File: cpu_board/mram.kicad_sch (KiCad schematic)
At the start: 12 parts, among them U4 EM064LXQADG13IS1T

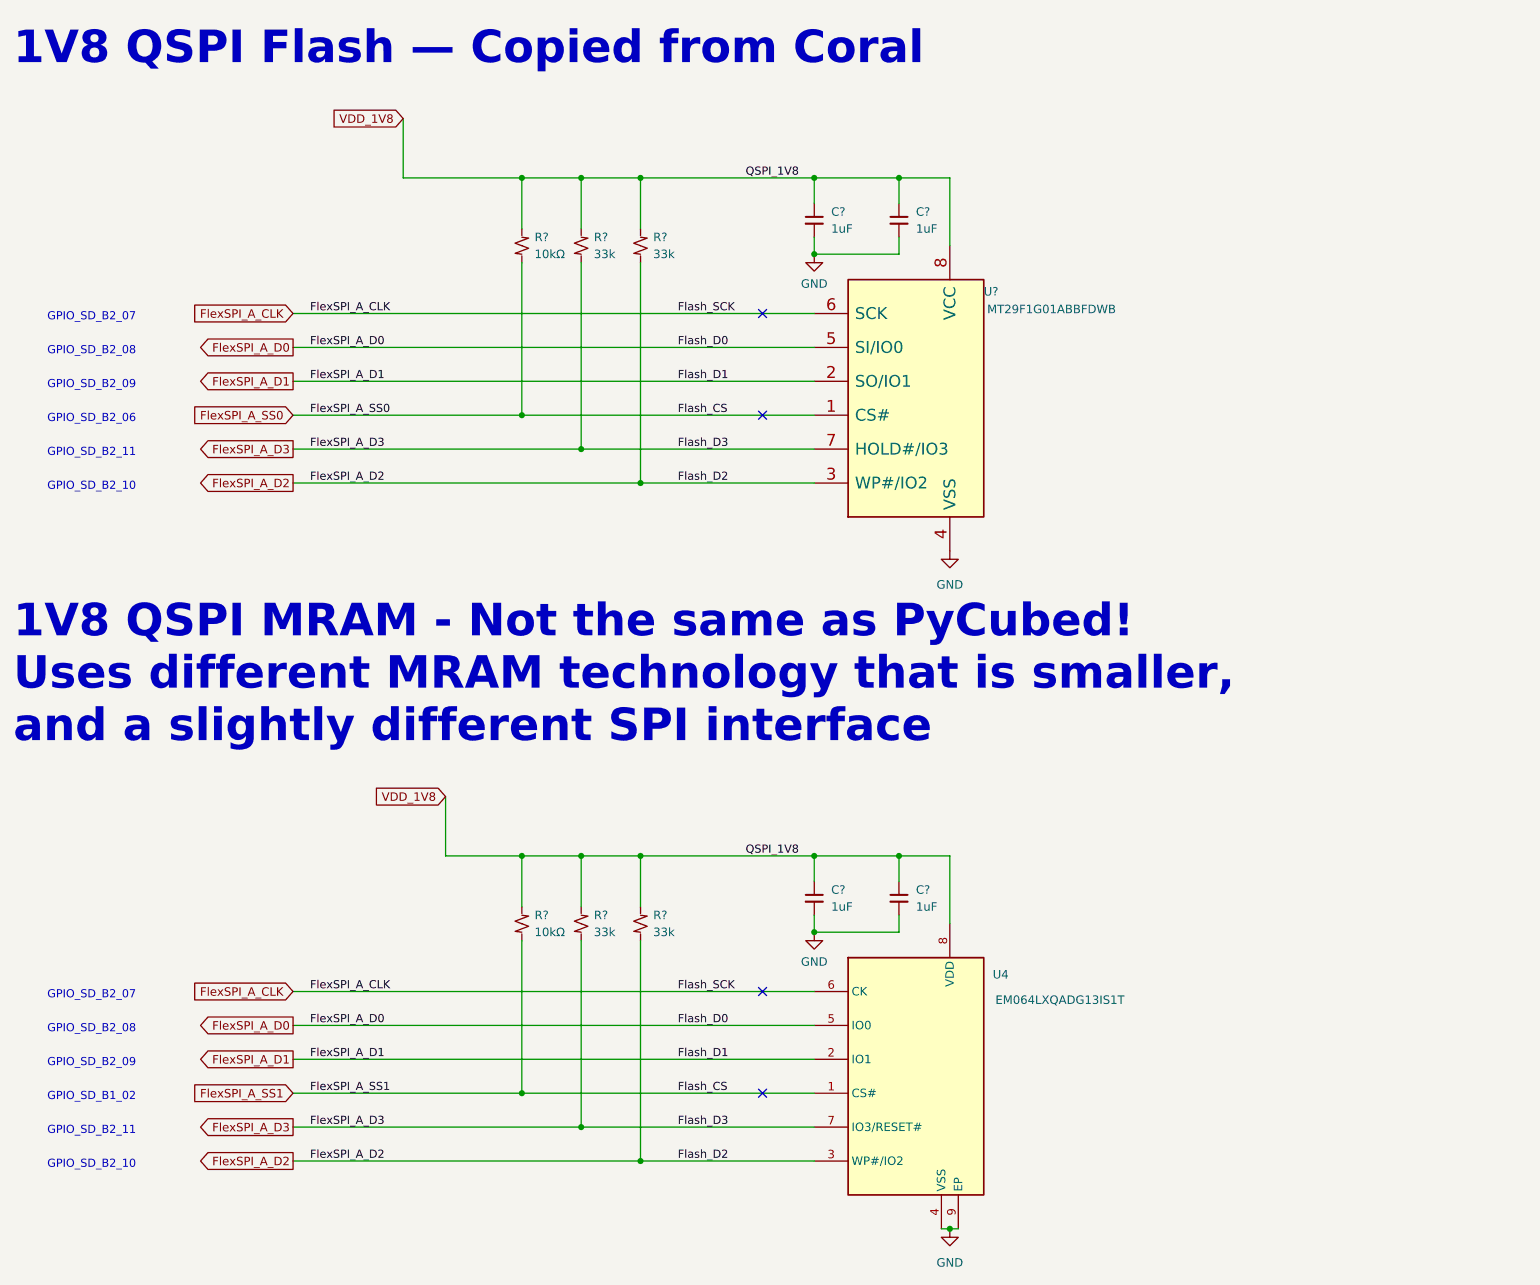
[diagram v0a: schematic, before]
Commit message: clean up board2board connector and organize TODOs
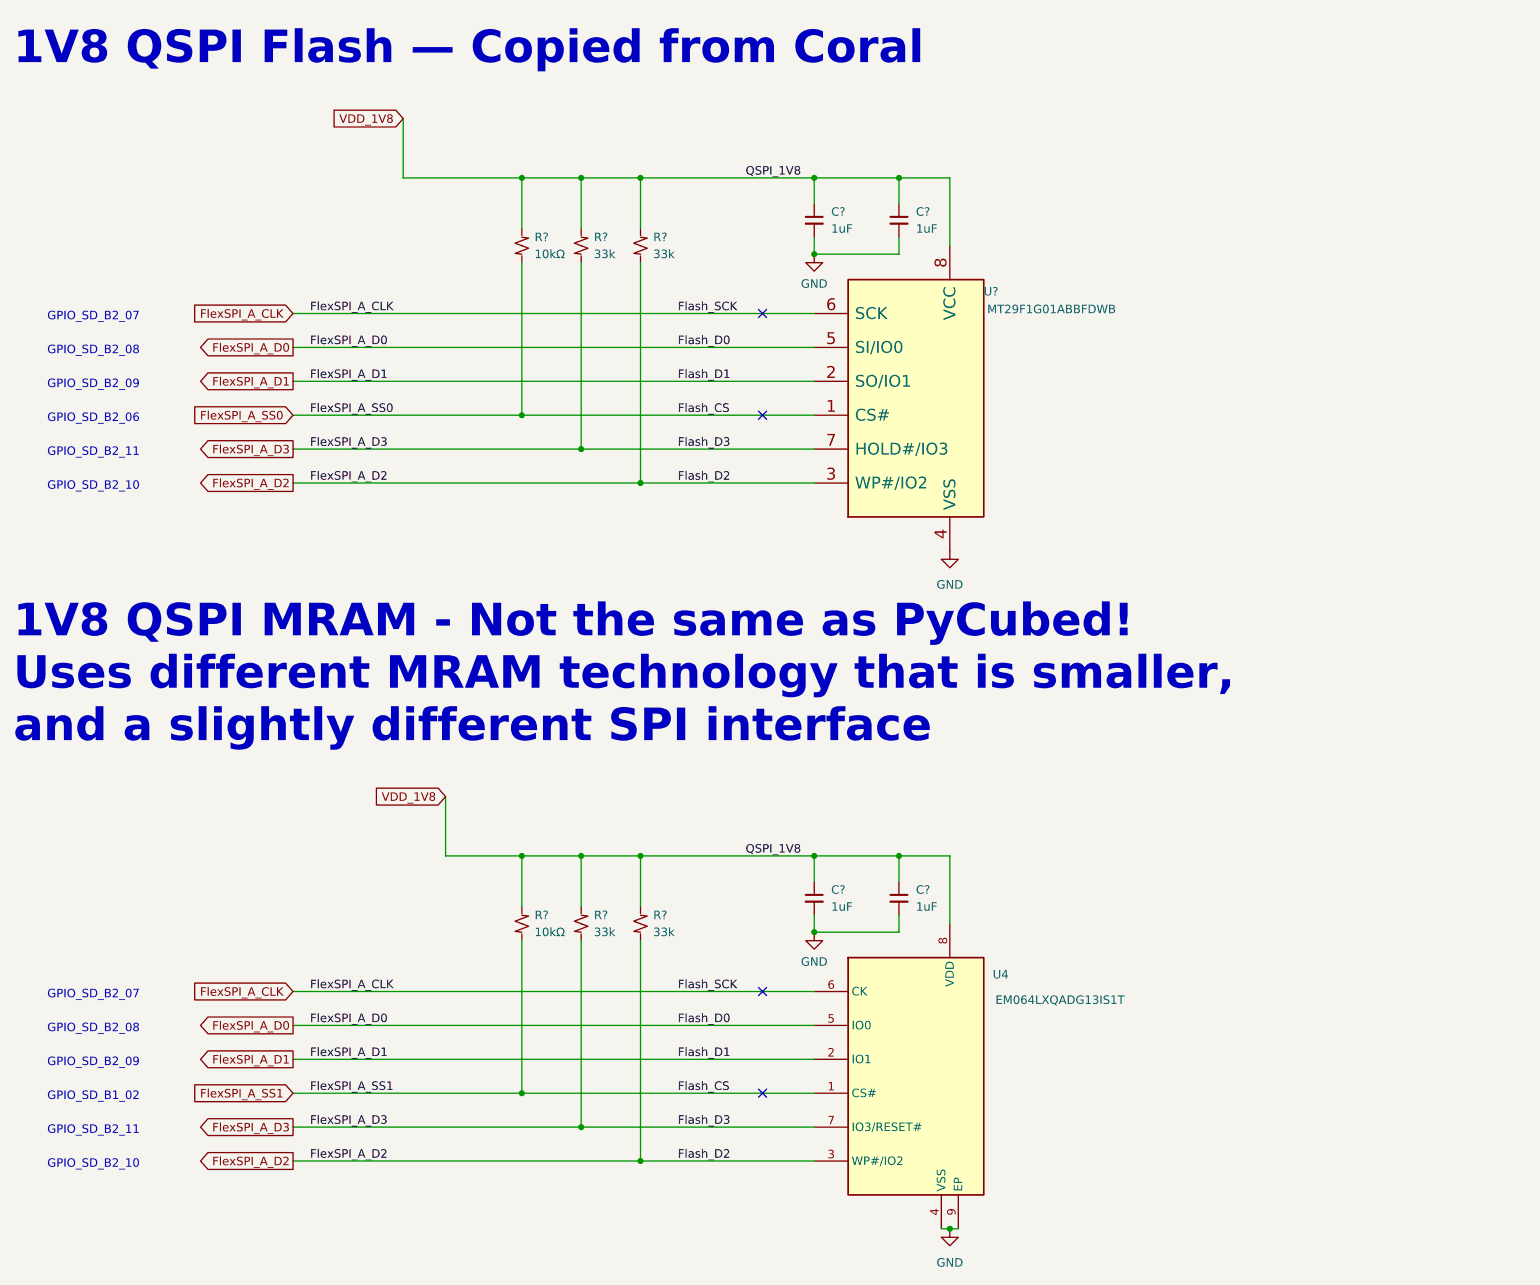
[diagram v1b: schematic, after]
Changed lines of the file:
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@@
   )
   (text "GPIO_SD_B2_10" (at 119.38 127 0)
-    (effects (font (size 1.2192 1.2192)) (justify left bottom))
+    (effects (font (size 1.27 1.27)) (justify left bottom))
   )
   (text "GPIO_SD_B2_10" (at 119.38 228.6 0)
-    (effects (font (size 1.2192 1.2192)) (justify left bottom))
+    (effects (font (size 1.27 1.27)) (justify left bottom))
   )
   (text "1V8 QSPI MRAM - Not the same as PyCubed! \nUses different MRAM technology that is smaller, \nand a slightly different SPI interface"
@@
   )
   (text "GPIO_SD_B2_08" (at 119.38 208.28 0)
-    (effects (font (size 1.2192 1.2192)) (justify left bottom))
+    (effects (font (size 1.27 1.27)) (justify left bottom))
   )
   (text "GPIO_SD_B2_08" (at 119.38 106.68 0)
-    (effects (font (size 1.2192 1.2192)) (justify left bottom))
+    (effects (font (size 1.27 1.27)) (justify left bottom))
   )
   (text "GPIO_SD_B2_06" (at 119.38 116.84 0)
-    (effects (font (size 1.2192 1.2192)) (justify left bottom))
+    (effects (font (size 1.27 1.27)) (justify left bottom))
   )
   (text "GPIO_SD_B2_07" (at 119.38 203.2 0)
-    (effects (font (size 1.2192 1.2192)) (justify left bottom))
+    (effects (font (size 1.27 1.27)) (justify left bottom))
   )
   (text "GPIO_SD_B1_02" (at 119.38 218.44 0)
-    (effects (font (size 1.2192 1.2192)) (justify left bottom))
+    (effects (font (size 1.27 1.27)) (justify left bottom))
   )
   (text "GPIO_SD_B2_09" (at 119.38 213.36 0)
-    (effects (font (size 1.2192 1.2192)) (justify left bottom))
+    (effects (font (size 1.27 1.27)) (justify left bottom))
   )
   (text "GPIO_SD_B2_09" (at 119.38 111.76 0)
-    (effects (font (size 1.2192 1.2192)) (justify left bottom))
+    (effects (font (size 1.27 1.27)) (justify left bottom))
   )
   (text "GPIO_SD_B2_11" (at 119.38 121.92 0)
-    (effects (font (size 1.2192 1.2192)) (justify left bottom))
+    (effects (font (size 1.27 1.27)) (justify left bottom))
   )
   (text "GPIO_SD_B2_07" (at 119.38 101.6 0)
-    (effects (font (size 1.2192 1.2192)) (justify left bottom))
+    (effects (font (size 1.27 1.27)) (justify left bottom))
   )
   (text "GPIO_SD_B2_11" (at 119.38 223.52 0)
-    (effects (font (size 1.2192 1.2192)) (justify left bottom))
+    (effects (font (size 1.27 1.27)) (justify left bottom))
   )
   (label "FlexSPI_A_D1" (at 158.75 110.49 0) (fields_autoplaced)
-    (effects (font (size 1.2192 1.2192)) (justify left bottom))
+    (effects (font (size 1.27 1.27)) (justify left bottom))
   )
   (label "Flash_SCK" (at 213.868 201.93 0) (fields_autoplaced)
-    (effects (font (size 1.2192 1.2192)) (justify left bottom))
+    (effects (font (size 1.27 1.27)) (justify left bottom))
   )
   (label "FlexSPI_A_D3" (at 158.75 120.65 0) (fields_autoplaced)
-    (effects (font (size 1.2192 1.2192)) (justify left bottom))
+    (effects (font (size 1.27 1.27)) (justify left bottom))
   )
   (label "FlexSPI_A_D2" (at 158.75 227.33 0) (fields_autoplaced)
-    (effects (font (size 1.2192 1.2192)) (justify left bottom))
+    (effects (font (size 1.27 1.27)) (justify left bottom))
   )
   (label "Flash_D1" (at 213.868 212.09 0) (fields_autoplaced)
-    (effects (font (size 1.2192 1.2192)) (justify left bottom))
+    (effects (font (size 1.27 1.27)) (justify left bottom))
   )
   (label "FlexSPI_A_D0" (at 158.75 105.41 0) (fields_autoplaced)
-    (effects (font (size 1.2192 1.2192)) (justify left bottom))
+    (effects (font (size 1.27 1.27)) (justify left bottom))
   )
   (label "Flash_D2" (at 213.868 227.33 0) (fields_autoplaced)
-    (effects (font (size 1.2192 1.2192)) (justify left bottom))
+    (effects (font (size 1.27 1.27)) (justify left bottom))
   )
   (label "FlexSPI_A_CLK" (at 158.75 100.33 0) (fields_autoplaced)
-    (effects (font (size 1.2192 1.2192)) (justify left bottom))
+    (effects (font (size 1.27 1.27)) (justify left bottom))
   )
   (label "FlexSPI_A_D1" (at 158.75 212.09 0) (fields_autoplaced)
-    (effects (font (size 1.2192 1.2192)) (justify left bottom))
+    (effects (font (size 1.27 1.27)) (justify left bottom))
   )
   (label "Flash_D2" (at 213.868 125.73 0) (fields_autoplaced)
-    (effects (font (size 1.2192 1.2192)) (justify left bottom))
+    (effects (font (size 1.27 1.27)) (justify left bottom))
   )
   (label "FlexSPI_A_D3" (at 158.75 222.25 0) (fields_autoplaced)
-    (effects (font (size 1.2192 1.2192)) (justify left bottom))
+    (effects (font (size 1.27 1.27)) (justify left bottom))
   )
   (label "Flash_D3" (at 213.868 222.25 0) (fields_autoplaced)
-    (effects (font (size 1.2192 1.2192)) (justify left bottom))
+    (effects (font (size 1.27 1.27)) (justify left bottom))
   )
   (label "FlexSPI_A_D0" (at 158.75 207.01 0) (fields_autoplaced)
-    (effects (font (size 1.2192 1.2192)) (justify left bottom))
+    (effects (font (size 1.27 1.27)) (justify left bottom))
   )
   (label "FlexSPI_A_SS0" (at 158.75 115.57 0) (fields_autoplaced)
-    (effects (font (size 1.2192 1.2192)) (justify left bottom))
+    (effects (font (size 1.27 1.27)) (justify left bottom))
   )
   (label "Flash_CS" (at 213.868 115.57 0) (fields_autoplaced)
-    (effects (font (size 1.2192 1.2192)) (justify left bottom))
+    (effects (font (size 1.27 1.27)) (justify left bottom))
   )
   (label "Flash_D0" (at 213.868 207.01 0) (fields_autoplaced)
-    (effects (font (size 1.2192 1.2192)) (justify left bottom))
+    (effects (font (size 1.27 1.27)) (justify left bottom))
   )
   (label "Flash_CS" (at 213.868 217.17 0) (fields_autoplaced)
-    (effects (font (size 1.2192 1.2192)) (justify left bottom))
+    (effects (font (size 1.27 1.27)) (justify left bottom))
   )
   (label "Flash_D3" (at 213.868 120.65 0) (fields_autoplaced)
-    (effects (font (size 1.2192 1.2192)) (justify left bottom))
+    (effects (font (size 1.27 1.27)) (justify left bottom))
   )
   (label "QSPI_1V8" (at 224.028 181.61 0) (fields_autoplaced)
-    (effects (font (size 1.2192 1.2192)) (justify left bottom))
+    (effects (font (size 1.27 1.27)) (justify left bottom))
   )
   (label "FlexSPI_A_SS1" (at 158.75 217.17 0) (fields_autoplaced)
-    (effects (font (size 1.2192 1.2192)) (justify left bottom))
+    (effects (font (size 1.27 1.27)) (justify left bottom))
   )
   (label "QSPI_1V8" (at 224.028 80.01 0) (fields_autoplaced)
-    (effects (font (size 1.2192 1.2192)) (justify left bottom))
+    (effects (font (size 1.27 1.27)) (justify left bottom))
   )
   (label "Flash_SCK" (at 213.868 100.33 0) (fields_autoplaced)
-    (effects (font (size 1.2192 1.2192)) (justify left bottom))
+    (effects (font (size 1.27 1.27)) (justify left bottom))
   )
   (label "Flash_D1" (at 213.868 110.49 0) (fields_autoplaced)
-    (effects (font (size 1.2192 1.2192)) (justify left bottom))
+    (effects (font (size 1.27 1.27)) (justify left bottom))
   )
   (label "FlexSPI_A_D2" (at 158.75 125.73 0) (fields_autoplaced)
-    (effects (font (size 1.2192 1.2192)) (justify left bottom))
+    (effects (font (size 1.27 1.27)) (justify left bottom))
   )
   (label "Flash_D0" (at 213.868 105.41 0) (fields_autoplaced)
-    (effects (font (size 1.2192 1.2192)) (justify left bottom))
+    (effects (font (size 1.27 1.27)) (justify left bottom))
   )
   (label "FlexSPI_A_CLK" (at 158.75 201.93 0) (fields_autoplaced)
-    (effects (font (size 1.2192 1.2192)) (justify left bottom))
+    (effects (font (size 1.27 1.27)) (justify left bottom))
   )
   (global_label "FlexSPI_A_CLK" (shape input) (at 156.21 100.33 180)

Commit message: route most of power distribution
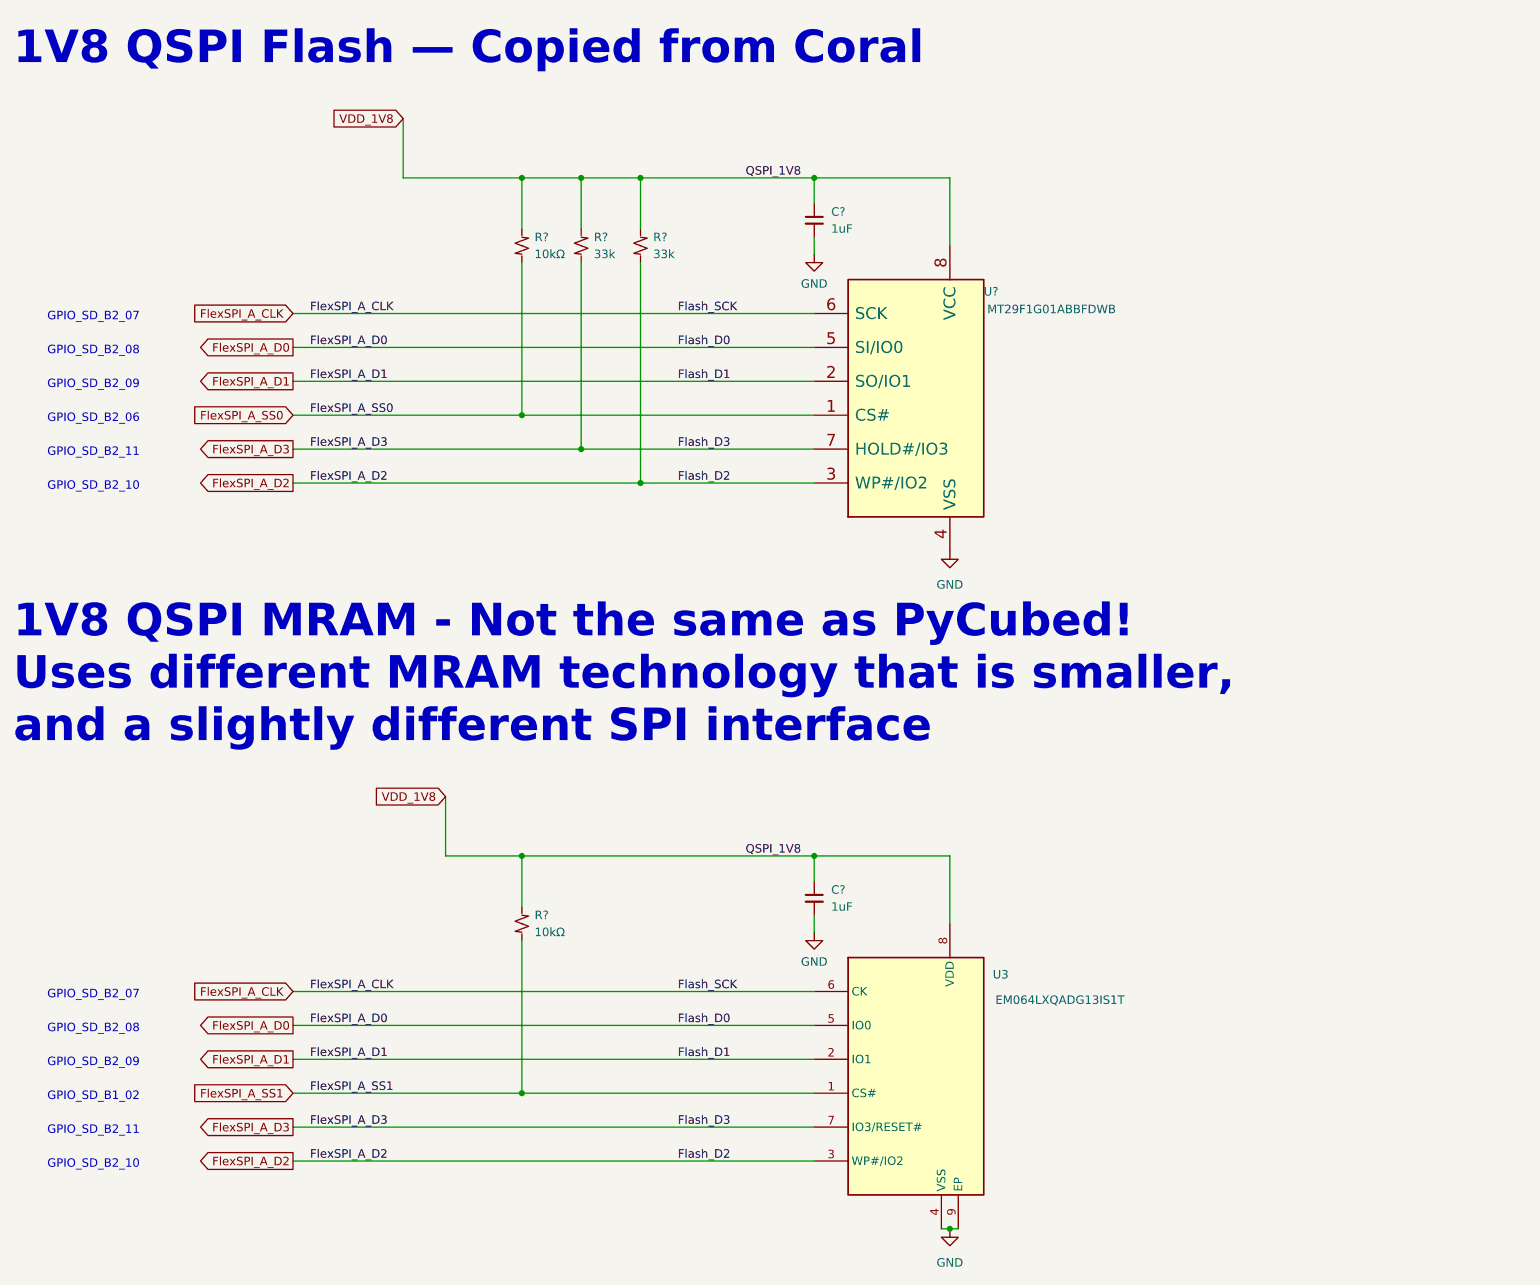
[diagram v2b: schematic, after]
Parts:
- removed C? (x2): 1uF, Capacitor_SMD:C_0402_1005Metric, symbol Device:C_Small
- removed R? (x2): 33k, Resistor_SMD:R_0402_1005Metric, symbol Device:R_Small_US
- renumbered U4 to U3
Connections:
- net FlexSPI_A_SS0: no longer R?.2, U3.1 (CS#)
- new net FlexSPI_A_SS1: R?.2, U3.1 (CS#)
- no-connect marks 4 -> 0

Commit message: continue work on fanout
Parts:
- C? (x2): footprint Capacitor_SMD:C_0402_1005Metric -> adcs:Perfect_0402
- R? (x4): footprint Resistor_SMD:R_0402_1005Metric -> adcs:Perfect_0402
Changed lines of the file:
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@@
       (effects (font (size 1.27 1.27)) (justify left))
     )
-    (property "Footprint" "Resistor_SMD:R_0402_1005Metric" (at 190.5 191.77 0)
+    (property "Footprint" "adcs:Perfect_0402" (at 190.5 191.77 0)
       (effects (font (size 1.27 1.27)) hide)
     )
@@
       (effects (font (size 1.27 1.27)) (justify left))
     )
-    (property "Footprint" "Resistor_SMD:R_0402_1005Metric" (at 199.39 90.17 0)
+    (property "Footprint" "adcs:Perfect_0402" (at 199.39 90.17 0)
       (effects (font (size 1.27 1.27)) hide)
     )
@@
       (effects (font (size 1.27 1.27)) (justify left))
     )
-    (property "Footprint" "Capacitor_SMD:C_0402_1005Metric" (at 234.315 86.36 0)
+    (property "Footprint" "adcs:Perfect_0402" (at 234.315 86.36 0)
       (effects (font (size 1.27 1.27)) hide)
     )
@@
       (effects (font (size 1.27 1.27)) hide)
     )
+    (property "DigiKey Part Number" "" (at 234.315 86.36 0)
+      (effects (font (size 1.27 1.27)) hide)
+    )
+    (property "Tolerance" "" (at 234.315 86.36 0)
+      (effects (font (size 1.27 1.27)))
+    )
+    (property "Power Rating" "" (at 234.315 86.36 0)
+      (effects (font (size 1.27 1.27)))
+    )
     (pin "1")
     (pin "2")
@@
       (effects (font (size 1.27 1.27)) (justify left))
     )
-    (property "Footprint" "Resistor_SMD:R_0402_1005Metric" (at 190.5 90.17 0)
+    (property "Footprint" "adcs:Perfect_0402" (at 190.5 90.17 0)
       (effects (font (size 1.27 1.27)) hide)
     )
@@
       (effects (font (size 1.27 1.27)) (justify left))
     )
-    (property "Footprint" "Capacitor_SMD:C_0402_1005Metric" (at 234.315 187.96 0)
+    (property "Footprint" "adcs:Perfect_0402" (at 234.315 187.96 0)
       (effects (font (size 1.27 1.27)) hide)
     )
@@
     (property "Footprint (for JLCPCB)" "0402" (at 234.315 187.96 0)
       (effects (font (size 1.27 1.27)) hide)
+    )
+    (property "DigiKey Part Number" "" (at 234.315 187.96 0)
+      (effects (font (size 1.27 1.27)) hide)
+    )
+    (property "Tolerance" "" (at 234.315 187.96 0)
+      (effects (font (size 1.27 1.27)))
+    )
+    (property "Power Rating" "" (at 234.315 187.96 0)
+      (effects (font (size 1.27 1.27)))
     )
     (pin "1")
@@
       (effects (font (size 1.27 1.27)) (justify left))
     )
-    (property "Footprint" "Resistor_SMD:R_0402_1005Metric" (at 208.28 90.17 0)
-      (effects (font (size 1.27 1.27)) hide)
-    )
+    (property "Footprint" "adcs:Perfect_0402" (at 208.28 90.17 0)
+      (effects (font (size 1.27 1.27)) hide)
+    )
